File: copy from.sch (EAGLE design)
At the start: 16 parts, among them J1 1X2-3.5MM, J2 1X2-3.5MM, J3 1X2-3.5MM

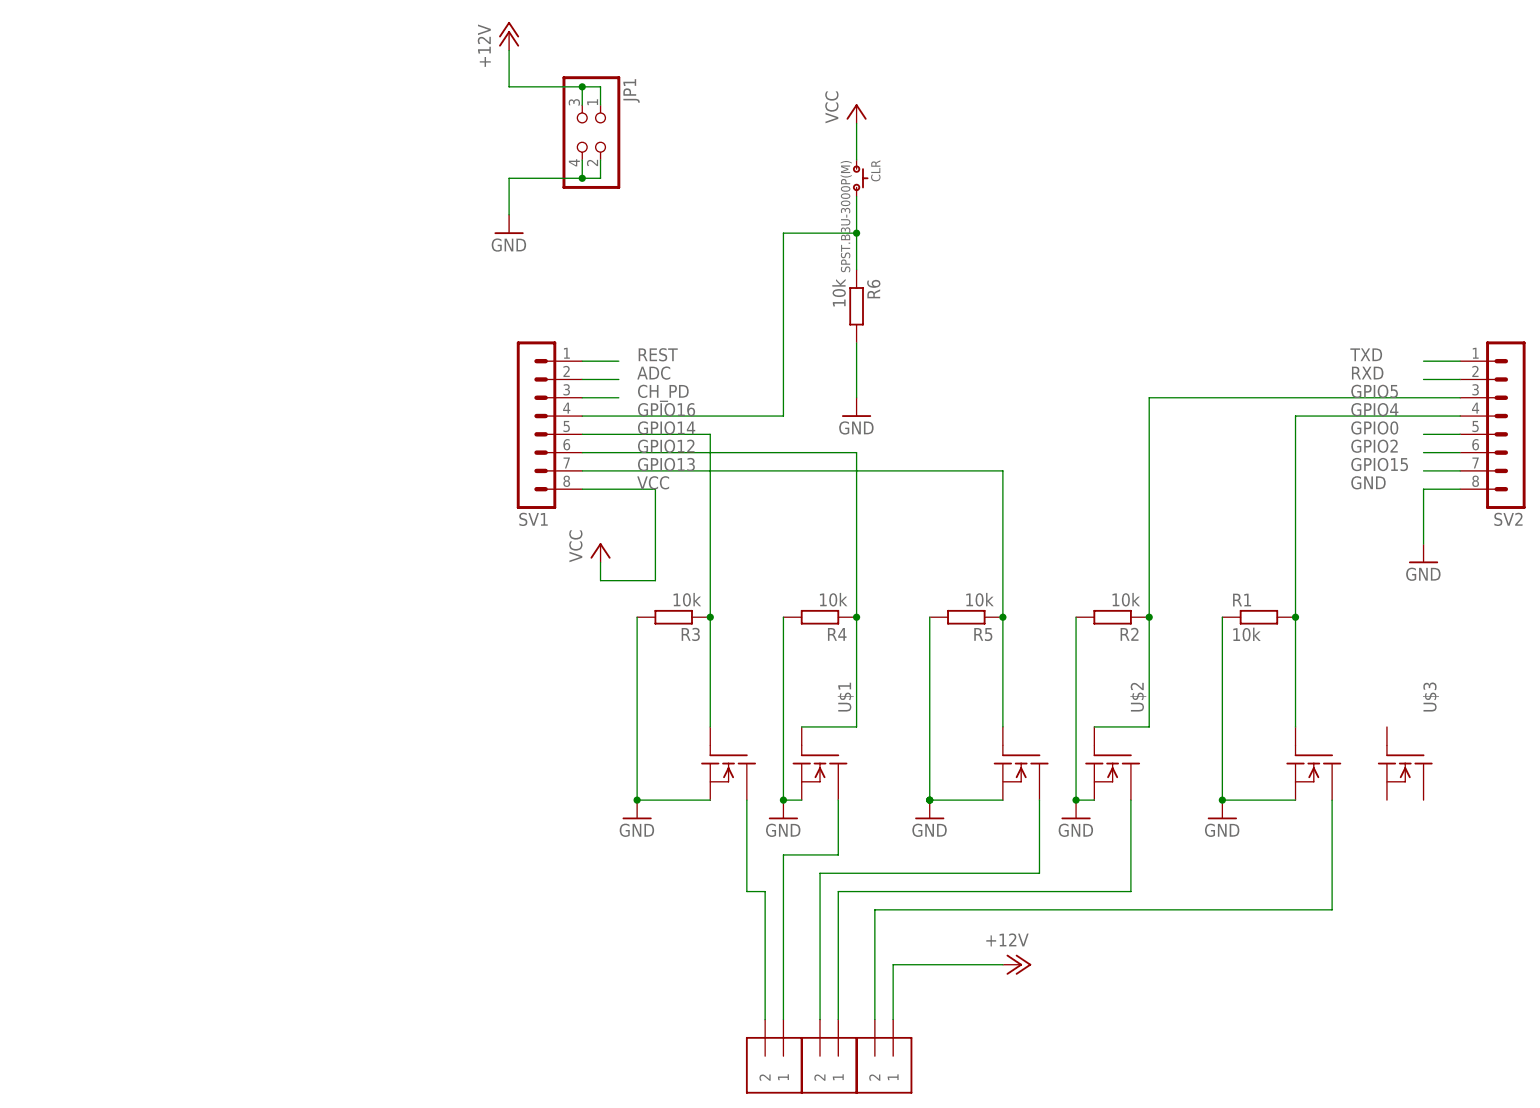
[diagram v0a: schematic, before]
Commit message: added an ftdi version
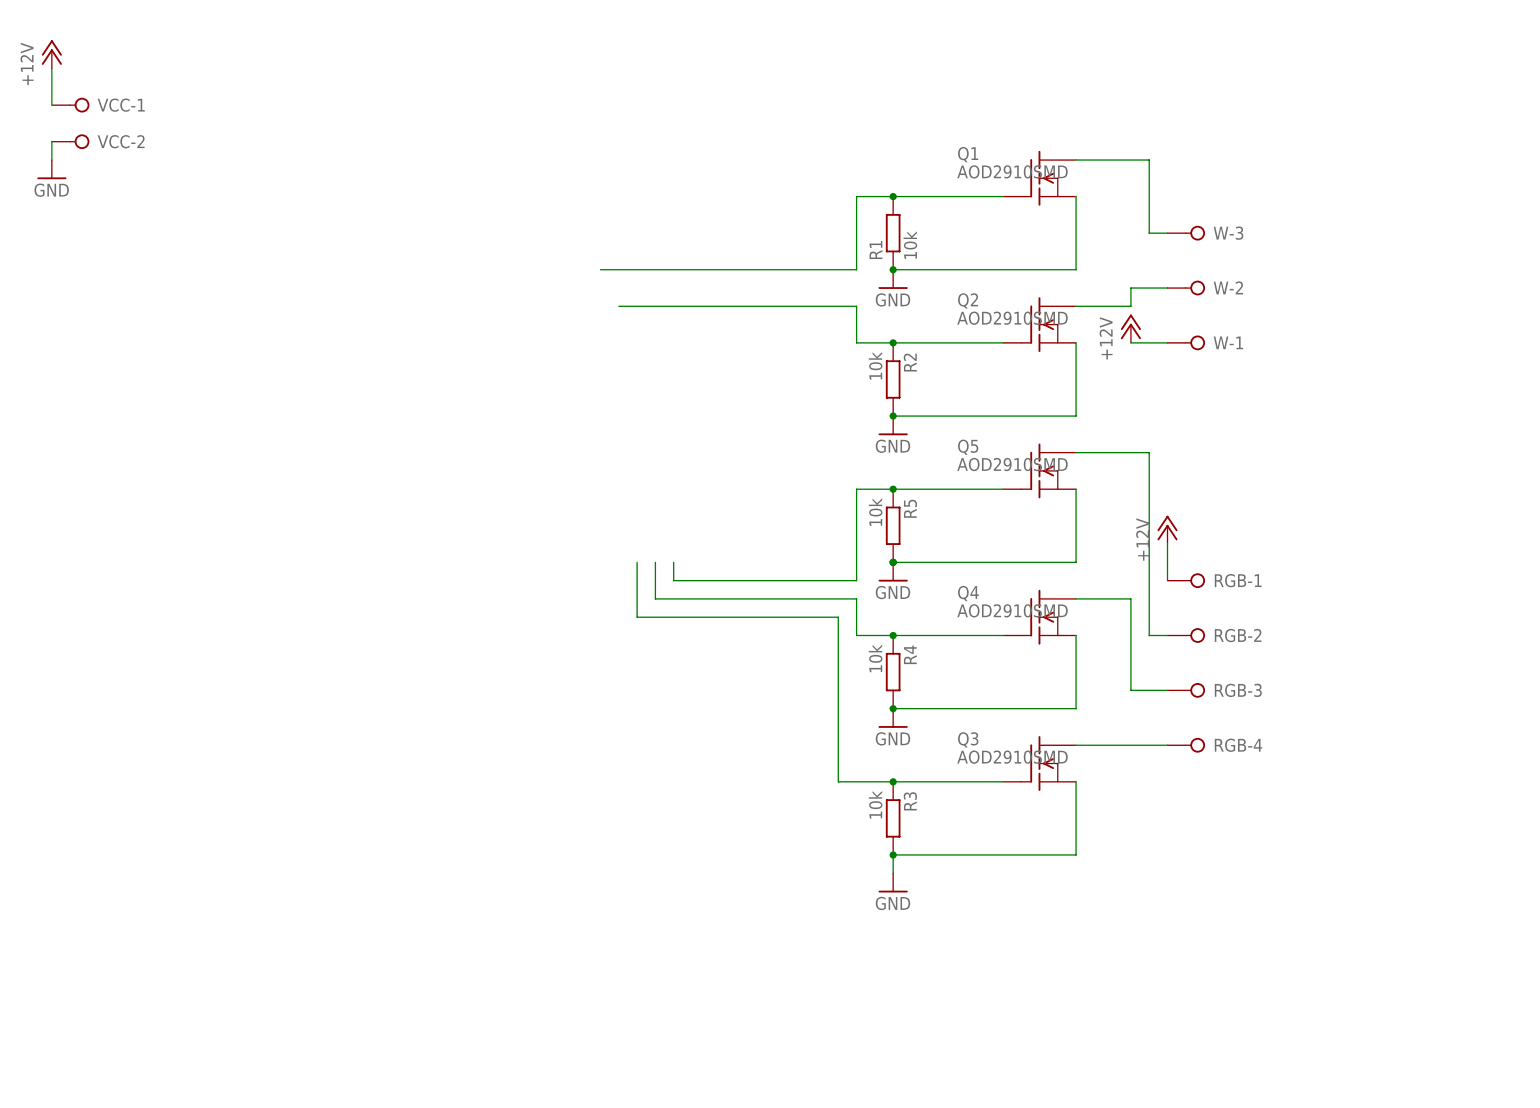
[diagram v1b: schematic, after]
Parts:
- removed CLR: SPST.B3U-3000P(M), omron:SPST.B3U-3000P(M)
- removed J1, J2, J3: 1X2-3.5MM, adafruit:1X2-3.5MM
- removed JP1: (no value), pinhead:PINHD-2X2
- removed R6: 10k, rcl:R-EU_R0805
- removed SV1, SV2: (no value), con-lstb:MA08-1
- removed U$1, U$2, U$3: AOD4806, esp12_RGBWW:AOD4806
- added Q1, Q2, Q3, Q4, Q5: AOD2910SMD, transistor-fet+irf7201:AOD2910SMD
- added RGB: (no value), con-wago-508:W237-04P
- added VCC: (no value), con-wago-508:W237-02P
- added W: (no value), con-wago-508:W237-03P
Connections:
- removed net ADC: SV1.2
- removed net CH_PD: SV1.3
- removed net GPIO0: SV2.5
- removed net GPIO12: R4.1, SV1.6, U$1.G
- removed net GPIO13: R5.1, SV1.7, U$2.G1
- removed net GPIO14: R3.1, SV1.5, U$1.G1
- removed net GPIO15: SV2.7
- removed net GPIO16: CLR.2, R6.1, SV1.4
- removed net GPIO2: SV2.6
- removed net GPIO4: R1.2, SV2.4, U$3.G1
- removed net GPIO5: R2.1, SV2.3, U$2.G
- removed net REST: SV1.1
- removed net RXD: SV2.2
- removed net TXD: SV2.1
- removed net VCC: CLR.1, SV1.8
- new net RGB-B: Q3.G, R3.1
- new net RGB-CW: Q2.G, R2.1
- new net RGB-G: Q4.G, R4.1
- new net RGB-R: Q5.G, R5.1
- new net RGB-WW: Q1.G, R1.2
- net +12V: now also RGB-1.KL, VCC-1.KL, W-1.KL; no longer J3.1, JP1.1, JP1.3
- net B: now also Q3.D, RGB-4.KL; no longer J1.2, U$1.D1
- net CW: now also Q2.D, W-2.KL; no longer J2.1, U$2.D
- net G: now also Q4.D, RGB-3.KL; no longer J1.1, U$1.D
- net GND: now also Q1.S, Q2.S, Q3.S, Q4.S, Q5.S, VCC-2.KL; no longer JP1.2, JP1.4, R6.2, SV2.8, U$1.S, U$1.S1, U$2.S, U$2.S1, U$3.S1
- net R: now also Q5.D, RGB-2.KL; no longer J2.2, U$2.D1
- net WW: now also Q1.D, W-3.KL; no longer J3.2, U$3.D1
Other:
- moved on the sheet: R1, R2, R3, R4, R5
